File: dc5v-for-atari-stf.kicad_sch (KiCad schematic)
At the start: 8 parts, among them J1 Conn_01x02, J2 Conn_01x06, J3 Adjustable MT3608 module, J4 Fixed 12V module, J5 Conn_01x02, SW1 Momentary or Latched

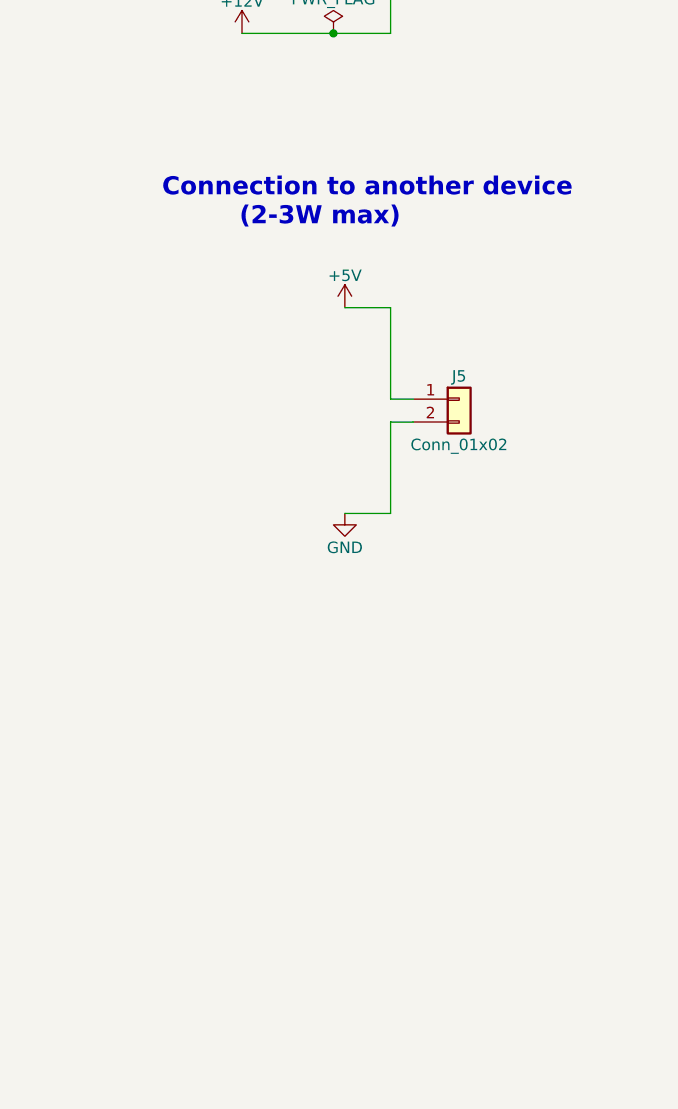
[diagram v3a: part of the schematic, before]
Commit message: associating footprints
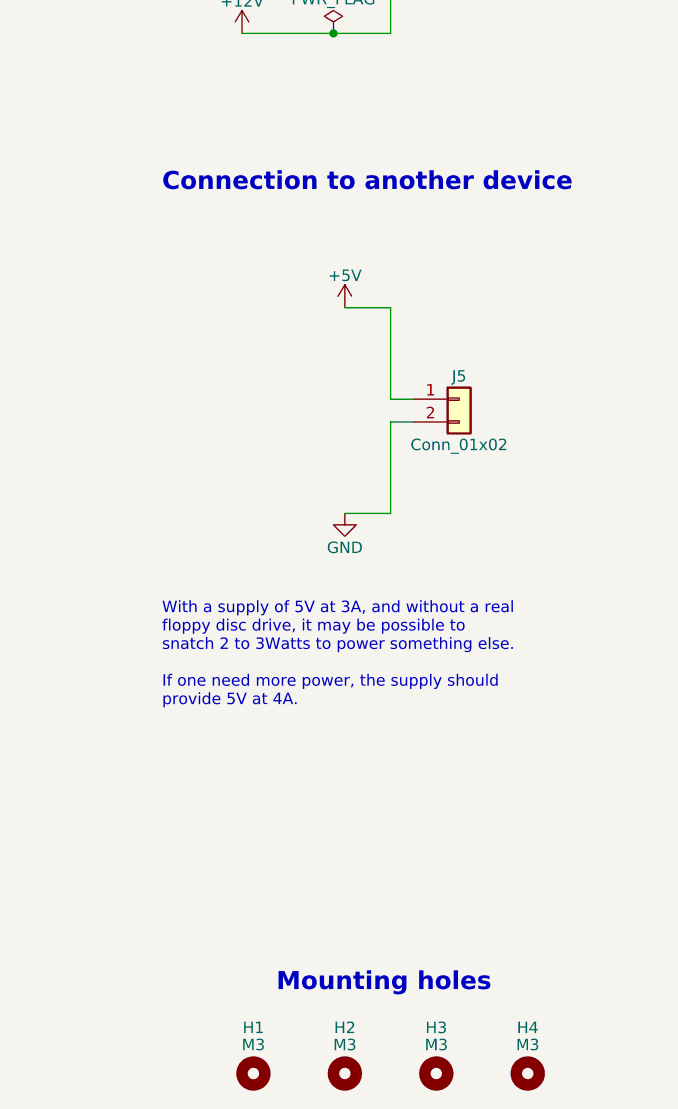
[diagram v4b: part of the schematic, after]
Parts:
- added H1, H2, H3, H4: M3, MountingHole:MountingHole_3.5mm, symbol Mechanical:MountingHole
- D1: footprint (none) -> LED_THT:LED_D3.0mm
- J1: footprint (none) -> commons-interconnect_THT:Fixed_Terminal_Blocks_Wurth_Elektronik_Serie_4122_7.00mm_Screwless_45degrees_1x02
- J2: footprint (none) -> Connector_PinHeader_2.54mm:PinHeader_1x06_P2.54mm_Vertical
- J3: footprint (none) -> assemblies_power_modules:module_mt3608_ajustable_output
- J4: footprint (none) -> assemblies_power_modules:module_dc_dc_step_up_12V_W10.16mm_H20.5mm_PinSocket_1x04_P2.54mm_Horizontal
- J5: footprint (none) -> Connector_PinHeader_2.54mm:PinHeader_1x02_P2.54mm_Vertical
- R1: footprint (none) -> commons-passives_THT:Passive_THT_resistor_W2.54mm_L12.70mm
- SW1: footprint (none) -> commons-interconnect_THT:combined_push_button_4pins_X_latched_button_6pins__2rows_W5_6mm_pitch_2.5_2.6mm
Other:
- note added: "Connection to another device"
- note added: "Mounting holes"
- note added: "With a supply of 5V at 3A, and without a real floppy disc drive, it may be possible to snatch 2 to 3Watts to power something else. If one need more power, the supply should provide 5V at 4A."
- note removed: "Connection to another device (2-3W max)"
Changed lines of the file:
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@@
+    (effects (font (size 1.27 1.27)) (justify left bottom))
+  )
+  (text "Mounting holes" (at 152.4 177.8 0)
+    (effects (font (size 2 2) (thickness 0.4) bold) (justify left bottom))
+  )
+  (text "With a supply of 5V at 3A, and without a real\nfloppy disc drive, it may be possible to\nsnatch 2 to 3Watts to power something else.\n\nIf one need more power, the supply should \nprovide 5V at 4A."
+    (at 139.7 146.05 0)
     (effects (font (size 1.27 1.27)) (justify left bottom))
   )
@@
     (effects (font (size 2 2) (thickness 0.4) bold) (justify left bottom))
   )
-  (text "Connection to another device\n         (2-3W max)" (at 139.7 92.71 0)
+  (text "Connection to another device" (at 139.7 88.9 0)
     (effects (font (size 2 2) (thickness 0.4) bold) (justify left bottom))
   )
@@
       (effects (font (size 1.27 1.27)) (justify left))
     )
-    (property "Footprint" "" (id 2) (at 49.53 111.76 0)
+    (property "Footprint" "assemblies_power_modules:module_mt3608_ajustable_output" (id 2) (at 49.53 111.76 0)
       (effects (font (size 1.27 1.27)) hide)
     )
@@
     (pin "4")
   )
+  (symbol (lib_id "Mechanical:MountingHole") (at 149.86 186.69 0) (unit 1)
+    (in_bom yes) (on_board yes)
+    (property "Reference" "H1" (id 0) (at 149.86 181.61 0))
+    (property "Value" "M3" (id 1) (at 149.86 183.515 0))
+    (property "Footprint" "MountingHole:MountingHole_3.5mm" (id 2) (at 149.86 186.69 0)
+      (effects (font (size 1.27 1.27)) hide)
+    )
+    (property "Datasheet" "~" (id 3) (at 149.86 186.69 0)
+      (effects (font (size 1.27 1.27)) hide)
+    )
+  )
   (symbol (lib_id "power:GND") (at 77.47 48.26 0) (unit 1)
     (in_bom yes) (on_board yes)
@@
     (pin "1")
   )
+  (symbol (lib_id "Mechanical:MountingHole") (at 160.02 186.69 0) (unit 1)
+    (in_bom yes) (on_board yes)
+    (property "Reference" "H2" (id 0) (at 160.02 181.61 0))
+    (property "Value" "M3" (id 1) (at 160.02 183.515 0))
+    (property "Footprint" "MountingHole:MountingHole_3.5mm" (id 2) (at 160.02 186.69 0)
+      (effects (font (size 1.27 1.27)) hide)
+    )
+    (property "Datasheet" "~" (id 3) (at 160.02 186.69 0)
+      (effects (font (size 1.27 1.27)) hide)
+    )
+  )
   (symbol (lib_id "Connector_Generic:Conn_01x06") (at 172.72 53.34 0) (unit 1)
     (in_bom yes) (on_board yes)
     (property "Reference" "J2" (id 0) (at 172.72 45.72 0))
     (property "Value" "Conn_01x06" (id 1) (at 172.72 63.5 0))
-    (property "Footprint" "" (id 2) (at 172.72 53.34 0)
+    (property "Footprint" "Connector_PinHeader_2.54mm:PinHeader_1x06_P2.54mm_Vertical" (id 2) (at 172.72 53.34 0)
       (effects (font (size 1.27 1.27)) hide)
     )
@@
     (pin "1")
   )
+  (symbol (lib_id "Mechanical:MountingHole") (at 170.18 186.69 0) (unit 1)
+    (in_bom yes) (on_board yes)
+    (property "Reference" "H3" (id 0) (at 170.18 181.61 0))
+    (property "Value" "M3" (id 1) (at 170.18 183.515 0))
+    (property "Footprint" "MountingHole:MountingHole_3.5mm" (id 2) (at 170.18 186.69 0)
+      (effects (font (size 1.27 1.27)) hide)
+    )
+    (property "Datasheet" "~" (id 3) (at 170.18 186.69 0)
+      (effects (font (size 1.27 1.27)) hide)
+    )
+  )
   (symbol (lib_id "Connector_Generic:Conn_01x02") (at 172.72 111.76 0) (unit 1)
     (in_bom yes) (on_board yes)
     (property "Reference" "J5" (id 0) (at 172.72 109.22 0))
     (property "Value" "Conn_01x02" (id 1) (at 172.72 116.84 0))
-    (property "Footprint" "" (id 2) (at 172.72 111.76 0)
+    (property "Footprint" "Connector_PinHeader_2.54mm:PinHeader_1x02_P2.54mm_Vertical" (id 2) (at 172.72 111.76 0)
       (effects (font (size 1.27 1.27)) hide)
     )
@@
       (effects (font (size 1.27 1.27)) (justify left))
     )
-    (property "Footprint" "" (id 2) (at 95.25 111.76 0)
+    (property "Footprint" "assemblies_power_modules:module_dc_dc_step_up_12V_W10.16mm_H20.5mm_PinSocket_1x04_P2.54mm_Horizontal" (id 2) (at 95.25 111.76 0)
       (effects (font (size 1.27 1.27)) hide)
     )
@@
     (property "Reference" "J1" (id 0) (at 90.17 35.56 0))
     (property "Value" "Conn_01x02" (id 1) (at 90.17 43.18 0))
-    (property "Footprint" "" (id 2) (at 90.17 38.1 0)
+    (property "Footprint" "commons-interconnect_THT:Fixed_Terminal_Blocks_Wurth_Elektronik_Serie_4122_7.00mm_Screwless_45degrees_1x02" (id 2) (at 90.17 38.1 0)
       (effects (font (size 1.27 1.27)) hide)
     )
@@
     )
     (property "Value" "Momentary or Latched" (id 1) (at 38.1 47.244 0))
-    (property "Footprint" "" (id 2) (at 38.1 40.64 0)
+    (property "Footprint" "commons-interconnect_THT:combined_push_button_4pins_X_latched_button_6pins__2rows_W5_6mm_pitch_2.5_2.6mm" (id 2) (at 38.1 40.64 0)
       (effects (font (size 1.27 1.27)) hide)
     )
@@
     (pin "1")
     (pin "2")
+  )
+  (symbol (lib_id "Mechanical:MountingHole") (at 180.34 186.69 0) (unit 1)
+    (in_bom yes) (on_board yes)
+    (property "Reference" "H4" (id 0) (at 180.34 181.61 0))
+    (property "Value" "M3" (id 1) (at 180.34 183.515 0))
+    (property "Footprint" "MountingHole:MountingHole_3.5mm" (id 2) (at 180.34 186.69 0)
+      (effects (font (size 1.27 1.27)) hide)
+    )
+    (property "Datasheet" "~" (id 3) (at 180.34 186.69 0)
+      (effects (font (size 1.27 1.27)) hide)
+    )
   )
   (symbol (lib_id "power:GND") (at 76.2 111.76 0) (unit 1)
@@
       (effects (font (size 1.27 1.27)) (justify right))
     )
-    (property "Footprint" "" (id 2) (at 66.04 45.72 0)
+    (property "Footprint" "LED_THT:LED_D3.0mm" (id 2) (at 66.04 45.72 0)
       (effects (font (size 1.27 1.27)) hide)
     )
@@
       (effects (font (size 1.27 1.27)) (justify right))
     )
-    (property "Footprint" "" (id 2) (at 53.34 45.72 0)
+    (property "Footprint" "commons-passives_THT:Passive_THT_resistor_W2.54mm_L12.70mm" (id 2) (at 53.34 45.72 0)
       (effects (font (size 1.27 1.27)) hide)
     )
@@
     )
     (path "/becb257d-9dab-4ba6-a653-48e5e5b84a78"
-      (reference "D1") (unit 1) (value "LED") (footprint "")
+      (reference "D1") (unit 1) (value "LED") (footprint "LED_THT:LED_D3.0mm")
+    )
+    (path "/42ff79f5-7aba-4233-be21-4072d4762c22"
+      (reference "H1") (unit 1) (value "M3") (footprint "MountingHole:MountingHole_3.5mm")
+    )
+    (path "/64eb2bcc-aeab-4a49-b917-135d8e744f1a"
+      (reference "H2") (unit 1) (value "M3") (footprint "MountingHole:MountingHole_3.5mm")
+    )
+    (path "/81a86fdf-3ef3-4dd0-8d8a-dd87141adc99"
+      (reference "H3") (unit 1) (value "M3") (footprint "MountingHole:MountingHole_3.5mm")
+    )
+    (path "/ab903420-ad3b-4c17-a4cf-d0f80ef06b1d"
+      (reference "H4") (unit 1) (value "M3") (footprint "MountingHole:MountingHole_3.5mm")
     )
     (path "/9d541d6f-313d-4469-a000-68242c1dd6d6"
-      (reference "J1") (unit 1) (value "Conn_01x02") (footprint "")
+      (reference "J1") (unit 1) (value "Conn_01x02") (footprint "commons-interconnect_THT:Fixed_Terminal_Blocks_Wurth_Elektronik_Serie_4122_7.00mm_Screwless_45degrees_1x02")
     )
     (path "/668b82fe-b542-4bd0-b2a5-5dae0ac43510"
-      (reference "J2") (unit 1) (value "Conn_01x06") (footprint "")
+      (reference "J2") (unit 1) (value "Conn_01x06") (footprint "Connector_PinHeader_2.54mm:PinHeader_1x06_P2.54mm_Vertical")
     )
     (path "/365f8d25-a297-4f89-a07e-59a6a6975ec7"
-      (reference "J3") (unit 1) (value "Adjustable MT3608 module") (footprint "")
+      (reference "J3") (unit 1) (value "Adjustable MT3608 module") (footprint "assemblies_power_modules:module_mt3608_ajustable_output")
     )
     (path "/91aeb66b-3414-4567-889a-6c6508c65350"
-      (reference "J4") (unit 1) (value "Fixed 12V module") (footprint "")
+      (reference "J4") (unit 1) (value "Fixed 12V module") (footprint "assemblies_power_modules:module_dc_dc_step_up_12V_W10.16mm_H20.5mm_PinSocket_1x04_P2.54mm_Horizontal")
     )
     (path "/843546ee-2f25-4c34-905b-947021231a4f"
-      (reference "J5") (unit 1) (value "Conn_01x02") (footprint "")
+      (reference "J5") (unit 1) (value "Conn_01x02") (footprint "Connector_PinHeader_2.54mm:PinHeader_1x02_P2.54mm_Vertical")
     )
     (path "/eda6fd21-2ea8-44f4-891c-53d66d7771f2"
-      (reference "R1") (unit 1) (value "2K") (footprint "")
+      (reference "R1") (unit 1) (value "2K") (footprint "commons-passives_THT:Passive_THT_resistor_W2.54mm_L12.70mm")
     )
     (path "/9fa2976a-cb33-4c73-9eda-224190576ec1"
-      (reference "SW1") (unit 1) (value "Momentary or Latched") (footprint "")
-    )
-  )
+      (reference "SW1") (unit 1) (value "Momentary or Latched") (footprint "commons-interconnect_THT:combined_push_button_4pins_X_latched_button_6pins__2rows_W5_6mm_pitch_2.5_2.6mm")
+    )
+  )

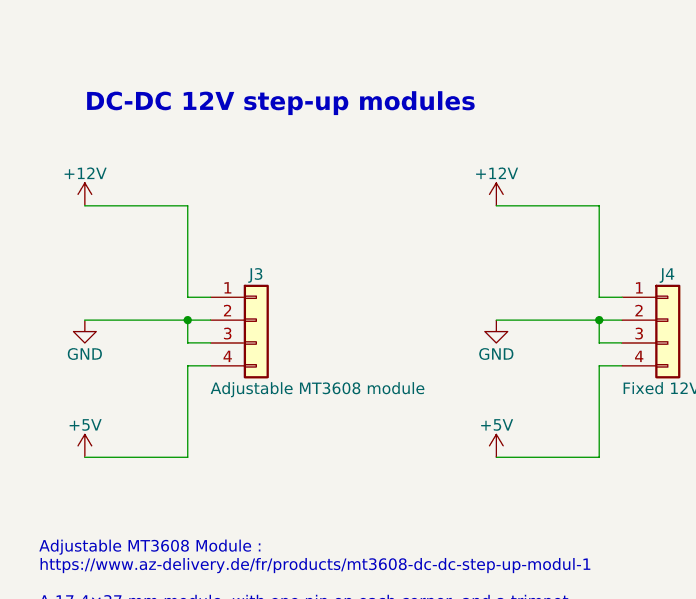
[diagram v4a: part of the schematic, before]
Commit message: pcb : layout, pcb edges
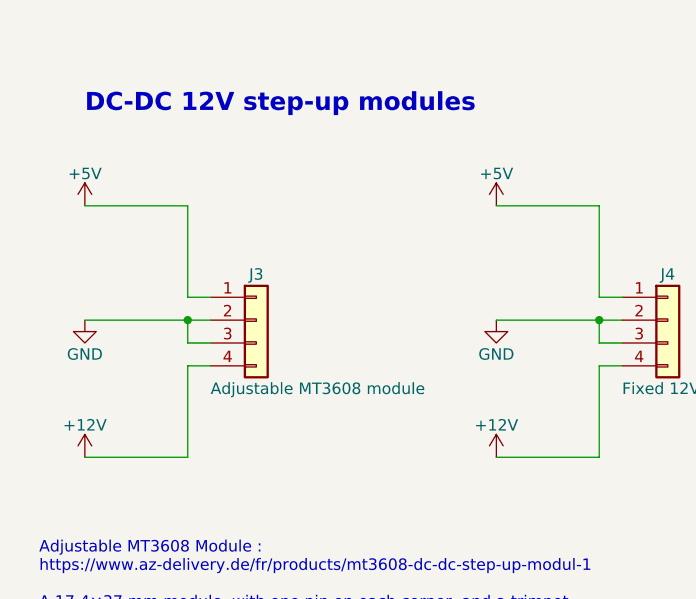
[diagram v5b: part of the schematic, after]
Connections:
- net +12V: now also J3.4 (Pin_4), J4.4 (Pin_4); no longer J3.1 (Pin_1), J4.1 (Pin_1)
- net +5V: now also J3.1 (Pin_1), J4.1 (Pin_1); no longer J3.4 (Pin_4), J4.4 (Pin_4)
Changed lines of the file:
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@@
     (pin "4")
   )
-  (symbol (lib_id "power:+5V") (at 76.2 127 0) (unit 1)
+  (symbol (lib_id "power:+5V") (at 76.2 99.06 0) (unit 1)
     (in_bom yes) (on_board yes)
-    (property "Reference" "#PWR013" (id 0) (at 76.2 130.81 0)
+    (property "Reference" "#PWR013" (id 0) (at 76.2 102.87 0)
       (effects (font (size 1.27 1.27)) hide)
     )
-    (property "Value" "+5V" (id 1) (at 76.2 123.444 0))
-    (property "Footprint" "" (id 2) (at 76.2 127 0)
+    (property "Value" "+5V" (id 1) (at 76.2 95.504 0))
+    (property "Footprint" "" (id 2) (at 76.2 99.06 0)
       (effects (font (size 1.27 1.27)) hide)
     )
-    (property "Datasheet" "" (id 3) (at 76.2 127 0)
+    (property "Datasheet" "" (id 3) (at 76.2 99.06 0)
       (effects (font (size 1.27 1.27)) hide)
     )
@@
     (pin "1")
   )
-  (symbol (lib_id "power:+5V") (at 30.48 127 0) (unit 1)
+  (symbol (lib_id "power:+5V") (at 30.48 99.06 0) (unit 1)
     (in_bom yes) (on_board yes)
-    (property "Reference" "#PWR012" (id 0) (at 30.48 130.81 0)
+    (property "Reference" "#PWR012" (id 0) (at 30.48 102.87 0)
       (effects (font (size 1.27 1.27)) hide)
     )
-    (property "Value" "+5V" (id 1) (at 30.48 123.444 0))
-    (property "Footprint" "" (id 2) (at 30.48 127 0)
+    (property "Value" "+5V" (id 1) (at 30.48 95.504 0))
+    (property "Footprint" "" (id 2) (at 30.48 99.06 0)
       (effects (font (size 1.27 1.27)) hide)
     )
-    (property "Datasheet" "" (id 3) (at 30.48 127 0)
+    (property "Datasheet" "" (id 3) (at 30.48 99.06 0)
       (effects (font (size 1.27 1.27)) hide)
     )
@@
     (pin "1")
   )
-  (symbol (lib_id "power:+12V") (at 76.2 99.06 0) (unit 1)
+  (symbol (lib_id "power:+12V") (at 76.2 127 0) (unit 1)
     (in_bom yes) (on_board yes)
-    (property "Reference" "#PWR07" (id 0) (at 76.2 102.87 0)
+    (property "Reference" "#PWR07" (id 0) (at 76.2 130.81 0)
       (effects (font (size 1.27 1.27)) hide)
     )
-    (property "Value" "+12V" (id 1) (at 76.2 95.504 0))
-    (property "Footprint" "" (id 2) (at 76.2 99.06 0)
+    (property "Value" "+12V" (id 1) (at 76.2 123.444 0))
+    (property "Footprint" "" (id 2) (at 76.2 127 0)
       (effects (font (size 1.27 1.27)) hide)
     )
-    (property "Datasheet" "" (id 3) (at 76.2 99.06 0)
+    (property "Datasheet" "" (id 3) (at 76.2 127 0)
       (effects (font (size 1.27 1.27)) hide)
     )
@@
     (pin "1")
   )
-  (symbol (lib_id "power:+12V") (at 30.48 99.06 0) (unit 1)
+  (symbol (lib_id "power:+12V") (at 30.48 127 0) (unit 1)
     (in_bom yes) (on_board yes)
-    (property "Reference" "#PWR06" (id 0) (at 30.48 102.87 0)
+    (property "Reference" "#PWR06" (id 0) (at 30.48 130.81 0)
       (effects (font (size 1.27 1.27)) hide)
     )
-    (property "Value" "+12V" (id 1) (at 30.48 95.504 0))
-    (property "Footprint" "" (id 2) (at 30.48 99.06 0)
+    (property "Value" "+12V" (id 1) (at 30.48 123.444 0))
+    (property "Footprint" "" (id 2) (at 30.48 127 0)
       (effects (font (size 1.27 1.27)) hide)
     )
-    (property "Datasheet" "" (id 3) (at 30.48 99.06 0)
+    (property "Datasheet" "" (id 3) (at 30.48 127 0)
       (effects (font (size 1.27 1.27)) hide)
     )

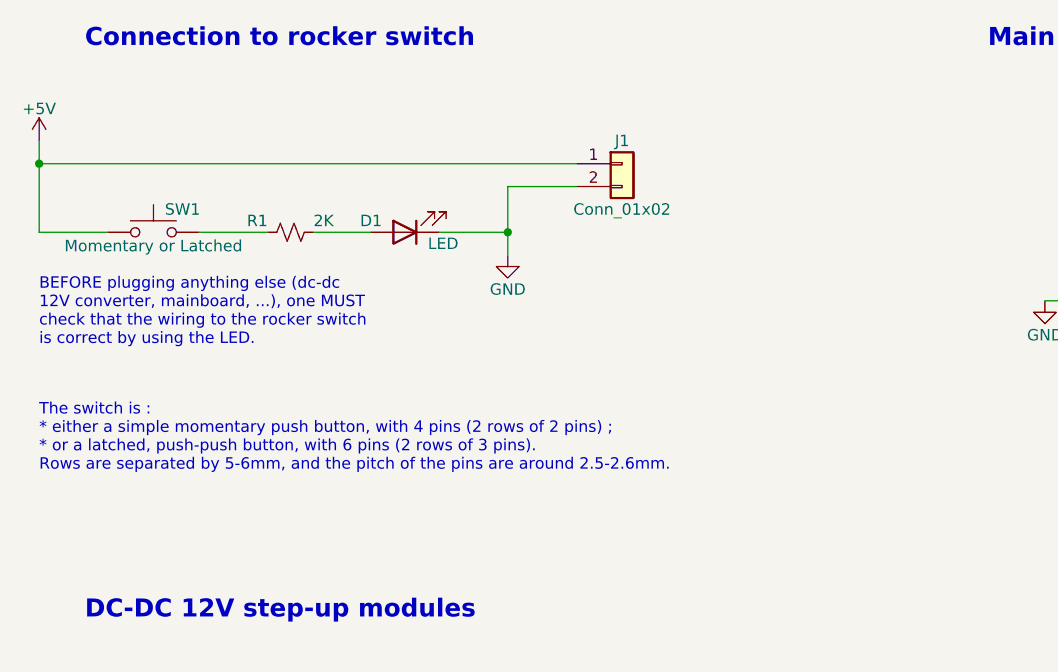
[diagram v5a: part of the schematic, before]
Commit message: schematic : provide alternative path to rocker switch, to optionnally protect with a fuse
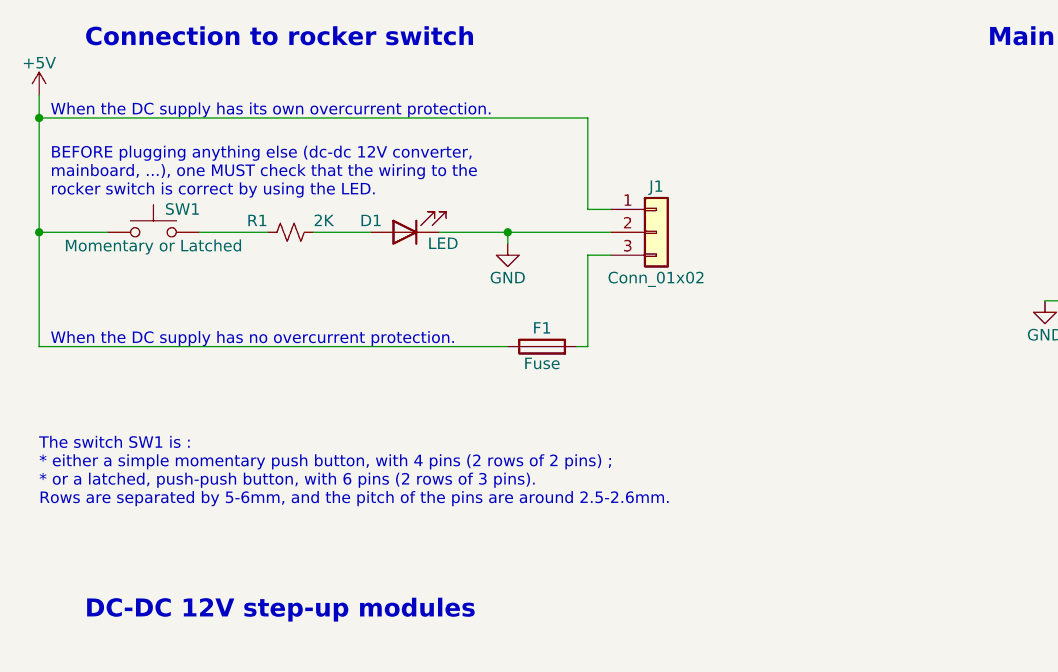
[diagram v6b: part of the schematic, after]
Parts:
- added F1: Fuse, symbol Device:Fuse
- J1: symbol Connector_Generic:Conn_01x02 -> Connector_Generic:Conn_01x03
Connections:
- net +5V: now also F1.1
- new net: F1.2, J1.3 (Pin_3)
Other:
- note added: "The switch SW1 is : * either a simple momentary push button, with 4 pins (2 rows of 2 pins) ; * or a latched, push-push button, with 6 pins (2 rows of 3 pins). Rows are separated by 5-6mm, and the pitch of the pins are around 2.5-2.6mm."
- note added: "When the DC supply has its own overcurrent protection."
- note added: "When the DC supply has no overcurrent protection."
- note removed: "The switch is : * either a simple momentary push button, with 4 pins (2 rows of 2 pins) ; * or a latched, push-push button, with 6 pins (2 rows of 3 pins). Rows are separated by 5-6mm, and the pitch of the pins are around 2.5-2.6mm."
